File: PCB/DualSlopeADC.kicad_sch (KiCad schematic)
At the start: 25 parts, among them J2 Conn_01x02_Pin, J3 Conn_01x02_Pin, J5 Conn_01x02_Pin, J6 Conn_01x02_Pin, J7 Conn_01x02_Pin, J8 Conn_01x02_Pin, J9 Conn_01x02_Pin, U1 CH32V003FxPx, U2 ADR4533, U3 AD8605ARTZ-R2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

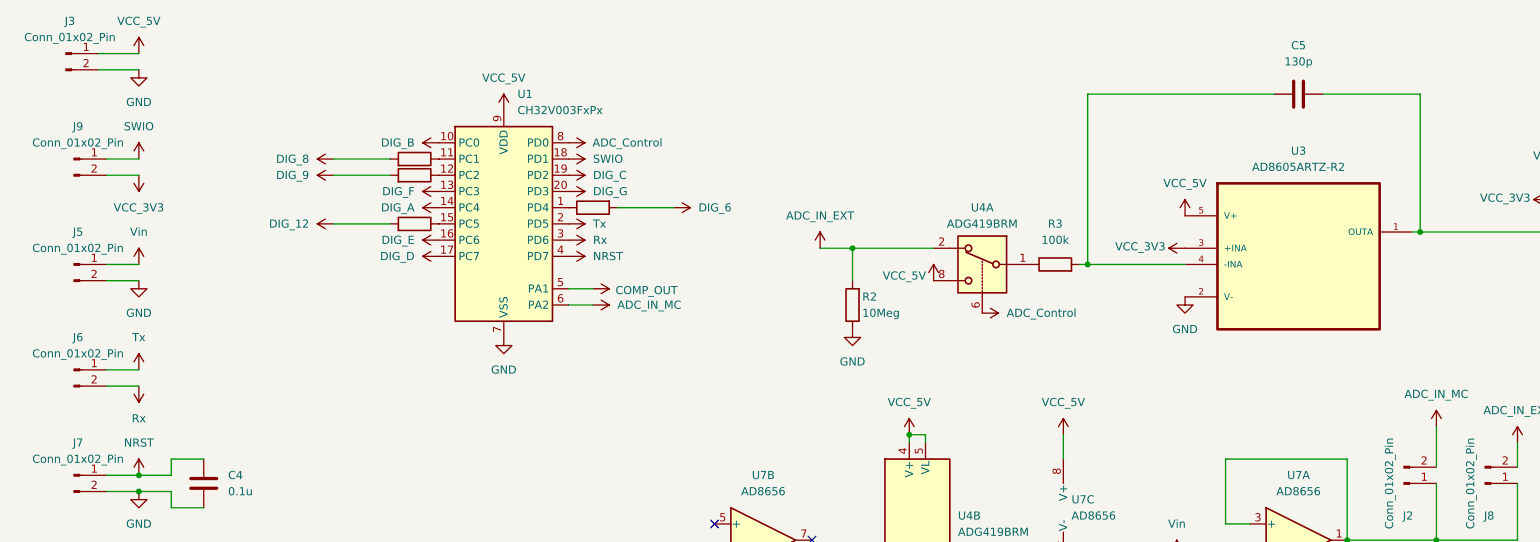
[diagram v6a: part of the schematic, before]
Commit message: Software ferrig, Timer einstellung auf basis das RC=100us, komplette gehirnschmelze wegen níchtlinearität durch offset sollte aber jetzt passen
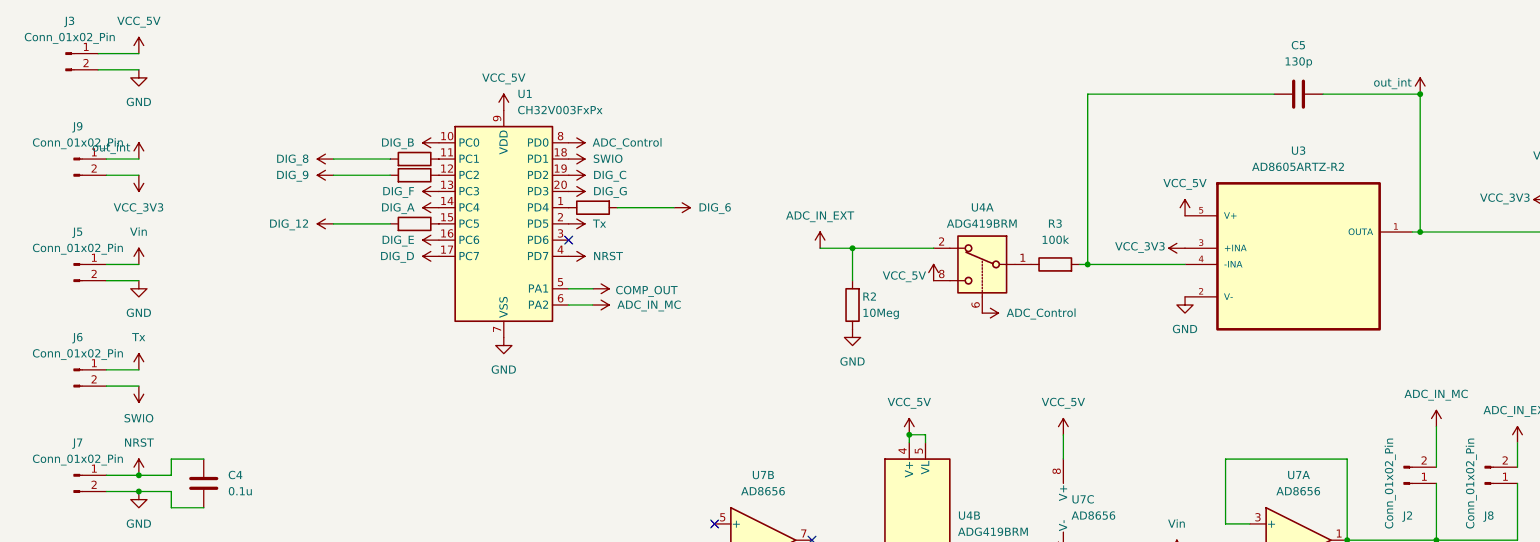
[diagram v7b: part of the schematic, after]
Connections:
- net SWIO: now also J6.2 (Pin_2); no longer J9.1 (Pin_1)
- net out_int: now reaches C5.2, U3.1 (OUTA), U5.4 (-)
- net out_int: now also J9.1 (Pin_1)
- net Rx: no longer names the net of U1.3 (PD6)
- net Rx: no longer J6.2 (Pin_2)
- no-connect marks 4 -> 5
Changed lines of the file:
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@@
 	)
 	(junction
+		(at 232.41 25.4)
+		(diameter 0)
+		(color 0 0 0 0)
+	)
+	(junction
 		(at 234.95 95.25)
 		(diameter 0)
@@
 		(at 121.92 97.79)
 	)
+	(no_connect
+		(at 99.06 48.26)
+	)
 	(wire
 		(pts
@@
 	(symbol
 		(lib_id "power:VCC")
-		(at 31.75 35.56 0)
+		(at 31.75 71.12 180)
 		(unit 1)
 		(exclude_from_sim no)
@@
 		(fields_autoplaced yes)
 		(property "Reference" "#PWR063"
-			(at 31.75 39.37 0)
+			(at 31.75 67.31 0)
 			(effects
 				(font
@@
 		)
 		(property "Value" "SWIO"
-			(at 31.75 30.48 0)
+			(at 31.75 76.2 0)
 			(effects
 				(font
@@
 		)
 		(property "Footprint" ""
-			(at 31.75 35.56 0)
+			(at 31.75 71.12 0)
 			(effects
 				(font
@@
 		)
 		(property "Datasheet" ""
-			(at 31.75 35.56 0)
+			(at 31.75 71.12 0)
 			(effects
 				(font
@@
 		)
 		(property "Description" "Power symbol creates a global label with name \"VCC\""
-			(at 31.75 35.56 0)
+			(at 31.75 71.12 0)
 			(effects
 				(font
@@
 	)
 	(symbol
-		(lib_id "power:VCC")
-		(at 99.06 48.26 270)
-		(unit 1)
-		(exclude_from_sim no)
-		(in_bom yes)
-		(on_board yes)
-		(dnp no)
-		(fields_autoplaced yes)
-		(property "Reference" "#PWR030"
-			(at 95.25 48.26 0)
-			(effects
-				(font
-					(size 1.27 1.27)
-				)
-				(hide yes)
-			)
-		)
-		(property "Value" "Rx"
-			(at 102.87 48.2599 90)
-			(effects
-				(font
-					(size 1.27 1.27)
-				)
-				(justify left)
-			)
-		)
-		(property "Footprint" ""
-			(at 99.06 48.26 0)
-			(effects
-				(font
-					(size 1.27 1.27)
-				)
-				(hide yes)
-			)
-		)
-		(property "Datasheet" ""
-			(at 99.06 48.26 0)
-			(effects
-				(font
-					(size 1.27 1.27)
-				)
-				(hide yes)
-			)
-		)
-		(property "Description" "Power symbol creates a global label with name \"VCC\""
-			(at 99.06 48.26 0)
-			(effects
-				(font
-					(size 1.27 1.27)
-				)
-				(hide yes)
-			)
-		)
-		(pin "1"
-		)
-		(instances
-			(project "DualSlopeADC"
-				(path "/283011ff-11cf-4a24-84b5-14acf4ed13a0"
-					(reference "#PWR030")
-					(unit 1)
-				)
-			)
-		)
-	)
-	(symbol
 		(lib_id "Device:R")
 		(at 175.26 52.07 90)
@@
 	)
 	(symbol
-		(lib_id "power:VCC")
-		(at 31.75 71.12 180)
-		(unit 1)
-		(exclude_from_sim no)
-		(in_bom yes)
-		(on_board yes)
-		(dnp no)
-		(fields_autoplaced yes)
-		(property "Reference" "#PWR025"
-			(at 31.75 67.31 0)
-			(effects
-				(font
-					(size 1.27 1.27)
-				)
-				(hide yes)
-			)
-		)
-		(property "Value" "Rx"
-			(at 31.75 76.2 0)
-			(effects
-				(font
-					(size 1.27 1.27)
-				)
-			)
-		)
-		(property "Footprint" ""
-			(at 31.75 71.12 0)
-			(effects
-				(font
-					(size 1.27 1.27)
-				)
-				(hide yes)
-			)
-		)
-		(property "Datasheet" ""
-			(at 31.75 71.12 0)
-			(effects
-				(font
-					(size 1.27 1.27)
-				)
-				(hide yes)
-			)
-		)
-		(property "Description" "Power symbol creates a global label with name \"VCC\""
-			(at 31.75 71.12 0)
-			(effects
-				(font
-					(size 1.27 1.27)
-				)
-				(hide yes)
-			)
-		)
-		(pin "1"
-		)
-		(instances
-			(project "DualSlopeADC"
-				(path "/283011ff-11cf-4a24-84b5-14acf4ed13a0"
-					(reference "#PWR025")
-					(unit 1)
-				)
-			)
-		)
-	)
-	(symbol
 		(lib_id "Device:C")
 		(at 66.04 128.27 0)
@@
 	)
 	(symbol
+		(lib_id "power:VCC")
+		(at 31.75 35.56 0)
+		(unit 1)
+		(exclude_from_sim no)
+		(in_bom yes)
+		(on_board yes)
+		(dnp no)
+		(property "Reference" "#PWR030"
+			(at 31.75 39.37 0)
+			(effects
+				(font
+					(size 1.27 1.27)
+				)
+				(hide yes)
+			)
+		)
+		(property "Value" "out_int"
+			(at 27.432 33.782 0)
+			(effects
+				(font
+					(size 1.27 1.27)
+				)
+			)
+		)
+		(property "Footprint" ""
+			(at 31.75 35.56 0)
+			(effects
+				(font
+					(size 1.27 1.27)
+				)
+				(hide yes)
+			)
+		)
+		(property "Datasheet" ""
+			(at 31.75 35.56 0)
+			(effects
+				(font
+					(size 1.27 1.27)
+				)
+				(hide yes)
+			)
+		)
+		(property "Description" "Power symbol creates a global label with name \"VCC\""
+			(at 31.75 35.56 0)
+			(effects
+				(font
+					(size 1.27 1.27)
+				)
+				(hide yes)
+			)
+		)
+		(pin "1"
+		)
+		(instances
+			(project "DualSlopeADC"
+				(path "/283011ff-11cf-4a24-84b5-14acf4ed13a0"
+					(reference "#PWR030")
+					(unit 1)
+				)
+			)
+		)
+	)
+	(symbol
 		(lib_id "power:GND")
 		(at 31.75 87.63 0)
@@
 					(unit 1)
 				)
+			)
+		)
+	)
+	(symbol
+		(lib_id "power:VCC")
+		(at 232.41 25.4 0)
+		(unit 1)
+		(exclude_from_sim no)
+		(in_bom yes)
+		(on_board yes)
+		(dnp no)
+		(property "Reference" "#PWR025"
+			(at 232.41 29.21 0)
+			(effects
+				(font
+					(size 1.27 1.27)
+				)
+				(hide yes)
+			)
+		)
+		(property "Value" "out_int"
+			(at 228.092 23.622 0)
+			(effects
+				(font
+					(size 1.27 1.27)
+				)
+			)
+		)
+		(property "Footprint" ""
+			(at 232.41 25.4 0)
+			(effects
+				(font
+					(size 1.27 1.27)
+				)
+				(hide yes)
+			)
+		)
+		(property "Datasheet" ""
+			(at 232.41 25.4 0)
+			(effects
+				(font
+					(size 1.27 1.27)
+				)
+				(hide yes)
+			)
+		)
+		(property "Description" "Power symbol creates a global label with name \"VCC\""
+			(at 232.41 25.4 0)
+			(effects
+				(font
+					(size 1.27 1.27)
+				)
+				(hide yes)
+			)
+		)
+		(pin "1"
+		)
+		(instances
+			(project "DualSlopeADC"
+				(path "/283011ff-11cf-4a24-84b5-14acf4ed13a0"
+					(reference "#PWR025")
+					(unit 1)
+				)

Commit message: Fehler in pCB behoben durch OP
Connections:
- net Vin: now also U7.3 (+); no longer U7.2 (-)
- net at J2.1 (Pin_1), J8.1 (Pin_1), U7.1: now also U7.2 (-); no longer U7.3 (+)
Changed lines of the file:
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@@
-	(wire
-		(pts
-			(xy 194.31 97.79) (xy 205.74 97.79)
-		)
-		(stroke
-			(width 0)
-			(type default)
-		)
-	)
 	(wire
 		(pts
@@
 	(wire
 		(pts
+			(xy 199.39 92.71) (xy 205.74 92.71)
+		)
+		(stroke
+			(width 0)
+			(type default)
+		)
+	)
+	(wire
+		(pts
 			(xy 26.67 52.07) (xy 31.75 52.07)
 		)
@@
 	(wire
 		(pts
+			(xy 199.39 97.79) (xy 199.39 92.71)
+		)
+		(stroke
+			(width 0)
+			(type default)
+		)
+	)
+	(wire
+		(pts
 			(xy 143.51 54.61) (xy 143.51 49.53)
 		)
@@
 	(wire
 		(pts
-			(xy 201.93 82.55) (xy 201.93 92.71)
+			(xy 201.93 82.55) (xy 201.93 97.79)
 		)
 		(stroke
@@
 	(wire
 		(pts
-			(xy 201.93 92.71) (xy 205.74 92.71)
-		)
-		(stroke
-			(width 0)
-			(type default)
-		)
-	)
-	(wire
-		(pts
 			(xy 152.4 78.74) (xy 154.94 78.74)
 		)
@@
 	(wire
 		(pts
+			(xy 194.31 97.79) (xy 199.39 97.79)
+		)
+		(stroke
+			(width 0)
+			(type default)
+		)
+	)
+	(wire
+		(pts
 			(xy 267.97 44.45) (xy 275.59 44.45)
 		)
@@
 		)
 		(stroke
+			(width 0)
+			(type default)
+		)
+	)
+	(wire
+		(pts
+			(xy 201.93 97.79) (xy 205.74 97.79)
+		)
+		(stroke
